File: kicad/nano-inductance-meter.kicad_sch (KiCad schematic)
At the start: 27 parts, among them J6 NOKIA5110_LCD, SW1 Calibrate, U1 MCP6004

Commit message: update
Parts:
- C2: value 100n -> 100nF
- Cref1: renamed from Cref; value 470n -> 470nF
- renumbered J6 to J1, JP2 to JP1, JP1 to JP2, Lx to Lx1, R19 to R10, R20 to R11, R21 to R12, R22 to R13, R7 to R2, R6 to R3, R2 to R4, R3 to R5, R4 to R6, R5 to R7, R17 to R8, R18 to R9
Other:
- note added: "Erősítő ~11x (~158Hz-től)"
- note added: "Schmitt-trigger"
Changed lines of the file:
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@@
 		(company "BT-Soft")
 	)
+	(text "Schmitt-trigger"
+		(exclude_from_sim no)
+		(at 161.29 48.006 0)
+		(effects
+			(font
+				(size 1.27 1.27)
+			)
+		)
+	)
 	(text "Vcc/2 (Vref)"
 		(exclude_from_sim no)
-		(at 118.364 71.374 0)
+		(at 118.872 96.012 0)
+		(effects
+			(font
+				(size 1.27 1.27)
+			)
+		)
+	)
+	(text "Erősítő ~11x\n(~158Hz-től)"
+		(exclude_from_sim no)
+		(at 126.746 53.086 0)
 		(effects
 			(font
@@
 		(on_board yes)
 		(dnp no)
-		(property "Reference" "J6"
+		(property "Reference" "J1"
 			(at 182.88 96.52 0)
 			(effects
@@
 			(project "nano-inductance-meter"
 				(path "/d4d5a955-4390-4c0c-a531-39dbbfc584c9"
-					(reference "J6")
+					(reference "J1")
 					(unit 1)
 				)
@@
 		(on_board yes)
 		(dnp no)
-		(property "Reference" "#PWR0131"
+		(property "Reference" "#PWR011"
 			(at 175.26 104.14 0)
 			(effects
@@
 			(project "nano-inductance-meter"
 				(path "/d4d5a955-4390-4c0c-a531-39dbbfc584c9"
-					(reference "#PWR0131")
+					(reference "#PWR011")
 					(unit 1)
 				)
@@
 		(on_board yes)
 		(dnp no)
-		(property "Reference" "R22"
+		(property "Reference" "R13"
 			(at 166.37 91.44 90)
 			(effects
@@
 			(project "nano-inductance-meter"
 				(path "/d4d5a955-4390-4c0c-a531-39dbbfc584c9"
-					(reference "R22")
+					(reference "R13")
 					(unit 1)
 				)
@@
 		(on_board yes)
 		(dnp no)
-		(property "Reference" "JP2"
+		(property "Reference" "JP1"
 			(at 148.1328 86.4616 90)
 			(effects
@@
 			(project "nano-inductance-meter"
 				(path "/d4d5a955-4390-4c0c-a531-39dbbfc584c9"
-					(reference "JP2")
+					(reference "JP1")
 					(unit 1)
 				)
@@
 		(on_board yes)
 		(dnp no)
-		(property "Reference" "#PWR0132"
+		(property "Reference" "#PWR09"
 			(at 147.32 95.25 0)
 			(effects
@@
 			(project "nano-inductance-meter"
 				(path "/d4d5a955-4390-4c0c-a531-39dbbfc584c9"
-					(reference "#PWR0132")
+					(reference "#PWR09")
 					(unit 1)
 				)
@@
 		(on_board yes)
 		(dnp no)
-		(property "Reference" "#PWR0133"
+		(property "Reference" "#PWR08"
 			(at 146.05 81.28 0)
 			(effects
@@
 			(project "nano-inductance-meter"
 				(path "/d4d5a955-4390-4c0c-a531-39dbbfc584c9"
-					(reference "#PWR0133")
+					(reference "#PWR08")
 					(unit 1)
 				)
@@
 		(on_board yes)
 		(dnp no)
-		(property "Reference" "R17"
+		(property "Reference" "R8"
 			(at 186.69 74.93 90)
 			(effects
@@
 			(project "nano-inductance-meter"
 				(path "/d4d5a955-4390-4c0c-a531-39dbbfc584c9"
-					(reference "R17")
+					(reference "R8")
 					(unit 1)
 				)
@@
 		(on_board yes)
 		(dnp no)
-		(property "Reference" "R18"
+		(property "Reference" "R9"
 			(at 186.69 77.47 90)
 			(effects
@@
 			(project "nano-inductance-meter"
 				(path "/d4d5a955-4390-4c0c-a531-39dbbfc584c9"
-					(reference "R18")
+					(reference "R9")
 					(unit 1)
 				)
@@
 		(on_board yes)
 		(dnp no)
-		(property "Reference" "R19"
+		(property "Reference" "R10"
 			(at 186.69 80.01 90)
 			(effects
@@
 			(project "nano-inductance-meter"
 				(path "/d4d5a955-4390-4c0c-a531-39dbbfc584c9"
-					(reference "R19")
+					(reference "R10")
 					(unit 1)
 				)
@@
 		(on_board yes)
 		(dnp no)
-		(property "Reference" "R20"
+		(property "Reference" "R11"
 			(at 186.69 82.55 90)
 			(effects
@@
 			(project "nano-inductance-meter"
 				(path "/d4d5a955-4390-4c0c-a531-39dbbfc584c9"
-					(reference "R20")
+					(reference "R11")
 					(unit 1)
 				)
@@
 		(on_board yes)
 		(dnp no)
-		(property "Reference" "R21"
+		(property "Reference" "R12"
 			(at 186.69 85.09 90)
 			(effects
@@
 			(project "nano-inductance-meter"
 				(path "/d4d5a955-4390-4c0c-a531-39dbbfc584c9"
-					(reference "R21")
+					(reference "R12")
 					(unit 1)
 				)
@@
 		(on_board yes)
 		(dnp no)
-		(property "Reference" "JP1"
+		(property "Reference" "JP2"
 			(at 171.45 69.723 0)
 			(effects
@@
 			(project "nano-inductance-meter"
 				(path "/d4d5a955-4390-4c0c-a531-39dbbfc584c9"
-					(reference "JP1")
+					(reference "JP2")
 					(unit 1)
 				)
@@
 		(dnp no)
 		(fields_autoplaced yes)
-		(property "Reference" "R6"
+		(property "Reference" "R3"
 			(at 90.17 96.5199 0)
 			(effects
@@
 			(project "nano-inductance-meter"
 				(path "/d4d5a955-4390-4c0c-a531-39dbbfc584c9"
-					(reference "R6")
+					(reference "R3")
 					(unit 1)
 				)
@@
 		(dnp no)
 		(fields_autoplaced yes)
-		(property "Reference" "Cref"
+		(property "Reference" "Cref1"
 			(at 97.79 49.5299 0)
 			(effects
@@
 			)
 		)
-		(property "Value" "470n"
+		(property "Value" "470nF"
 			(at 97.79 52.0699 0)
 			(effects
@@
 			(project "nano-inductance-meter"
 				(path "/d4d5a955-4390-4c0c-a531-39dbbfc584c9"
-					(reference "Cref")
+					(reference "Cref1")
 					(unit 1)
 				)
@@
 		(on_board yes)
 		(dnp no)
-		(property "Reference" "#PWR08"
+		(property "Reference" "#PWR03"
 			(at 53.34 45.72 0)
 			(effects
@@
 			(project "nano-inductance-meter"
 				(path "/d4d5a955-4390-4c0c-a531-39dbbfc584c9"
-					(reference "#PWR08")
+					(reference "#PWR03")
 					(unit 1)
 				)
@@
 		(on_board yes)
 		(dnp no)
-		(property "Reference" "#PWR09"
+		(property "Reference" "#PWR010"
 			(at 163.83 90.17 0)
 			(effects
@@
 			(project "nano-inductance-meter"
 				(path "/d4d5a955-4390-4c0c-a531-39dbbfc584c9"
-					(reference "#PWR09")
+					(reference "#PWR010")
 					(unit 1)
 				)
@@
 		(on_board yes)
 		(dnp no)
-		(property "Reference" "R5"
+		(property "Reference" "R7"
 			(at 149.352 23.114 90)
 			(effects
@@
 			(project "nano-inductance-meter"
 				(path "/d4d5a955-4390-4c0c-a531-39dbbfc584c9"
-					(reference "R5")
+					(reference "R7")
 					(unit 1)
 				)
@@
 		(dnp no)
 		(fields_autoplaced yes)
-		(property "Reference" "R7"
+		(property "Reference" "R2"
 			(at 90.17 82.5499 0)
 			(effects
@@
 			(project "nano-inductance-meter"
 				(path "/d4d5a955-4390-4c0c-a531-39dbbfc584c9"
-					(reference "R7")
+					(reference "R2")
 					(unit 1)
 				)
@@
 		(dnp no)
 		(fields_autoplaced yes)
-		(property "Reference" "Lx"
+		(property "Reference" "Lx1"
 			(at 81.28 49.5299 0)
 			(effects
@@
 			(project ""
 				(path "/d4d5a955-4390-4c0c-a531-39dbbfc584c9"
-					(reference "Lx")
+					(reference "Lx1")
 					(unit 1)
 				)
@@
 			)
 		)
-		(property "Value" "100n"
+		(property "Value" "100nF"
 			(at 115.57 64.7699 0)
 			(effects
@@
 		(dnp no)
 		(fields_autoplaced yes)
-		(property "Reference" "R2"
+		(property "Reference" "R4"
 			(at 114.3 53.3399 0)
 			(effects
@@
 			(project "nano-inductance-meter"
 				(path "/d4d5a955-4390-4c0c-a531-39dbbfc584c9"
-					(reference "R2")
+					(reference "R4")
 					(unit 1)
 				)
@@
 		(on_board yes)
 		(dnp no)
-		(property "Reference" "#PWR02"
+		(property "Reference" "#PWR06"
 			(at 87.63 80.01 0)
 			(effects
@@
 			(project ""
 				(path "/d4d5a955-4390-4c0c-a531-39dbbfc584c9"
-					(reference "#PWR02")
+					(reference "#PWR06")
 					(unit 1)
 				)
@@
 		(dnp no)
 		(fields_autoplaced yes)
-		(property "Reference" "R4"
+		(property "Reference" "R6"
 			(at 134.62 31.75 90)
 			(effects
@@
 			(project "nano-inductance-meter"
 				(path "/d4d5a955-4390-4c0c-a531-39dbbfc584c9"
-					(reference "R4")
+					(reference "R6")
 					(unit 1)
 				)
@@
 		(dnp no)
 		(fields_autoplaced yes)
-		(property "Reference" "#PWR04"
+		(property "Reference" "#PWR05"
 			(at 77.47 113.03 0)
 			(effects
@@
 			(project "nano-inductance-meter"
 				(path "/d4d5a955-4390-4c0c-a531-39dbbfc584c9"
-					(reference "#PWR04")
+					(reference "#PWR05")
 					(unit 1)
 				)
@@
 		(dnp no)
 		(fields_autoplaced yes)
-		(property "Reference" "R3"
+		(property "Reference" "R5"
 			(at 121.92 41.91 90)
 			(effects
@@
 			(project "nano-inductance-meter"
 				(path "/d4d5a955-4390-4c0c-a531-39dbbfc584c9"
-					(reference "R3")
+					(reference "R5")
 					(unit 1)
 				)
@@
 		(dnp no)
 		(fields_autoplaced yes)
-		(property "Reference" "#PWR06"
+		(property "Reference" "#PWR02"
 			(at 52.07 107.95 0)
 			(effects
@@
 			(project "nano-inductance-meter"
 				(path "/d4d5a955-4390-4c0c-a531-39dbbfc584c9"
-					(reference "#PWR06")
+					(reference "#PWR02")
 					(unit 1)
 				)
@@
 		(on_board yes)
 		(dnp no)
-		(property "Reference" "#PWR05"
+		(property "Reference" "#PWR04"
 			(at 55.88 45.72 0)
 			(effects
@@
 			(project "nano-inductance-meter"
 				(path "/d4d5a955-4390-4c0c-a531-39dbbfc584c9"
-					(reference "#PWR05")
+					(reference "#PWR04")
 					(unit 1)
 				)
@@
 		(dnp no)
 		(fields_autoplaced yes)
-		(property "Reference" "#PWR07"
+		(property "Reference" "#PWR01"
 			(at 22.86 67.31 0)
 			(effects
@@
 			(project "nano-inductance-meter"
 				(path "/d4d5a955-4390-4c0c-a531-39dbbfc584c9"
-					(reference "#PWR07")
+					(reference "#PWR01")
 					(unit 1)
 				)
@@
 		(dnp no)
 		(fields_autoplaced yes)
-		(property "Reference" "#PWR03"
+		(property "Reference" "#PWR07"
 			(at 87.63 113.03 0)
 			(effects
@@
 			(project ""
 				(path "/d4d5a955-4390-4c0c-a531-39dbbfc584c9"
-					(reference "#PWR03")
+					(reference "#PWR07")
 					(unit 1)
 				)

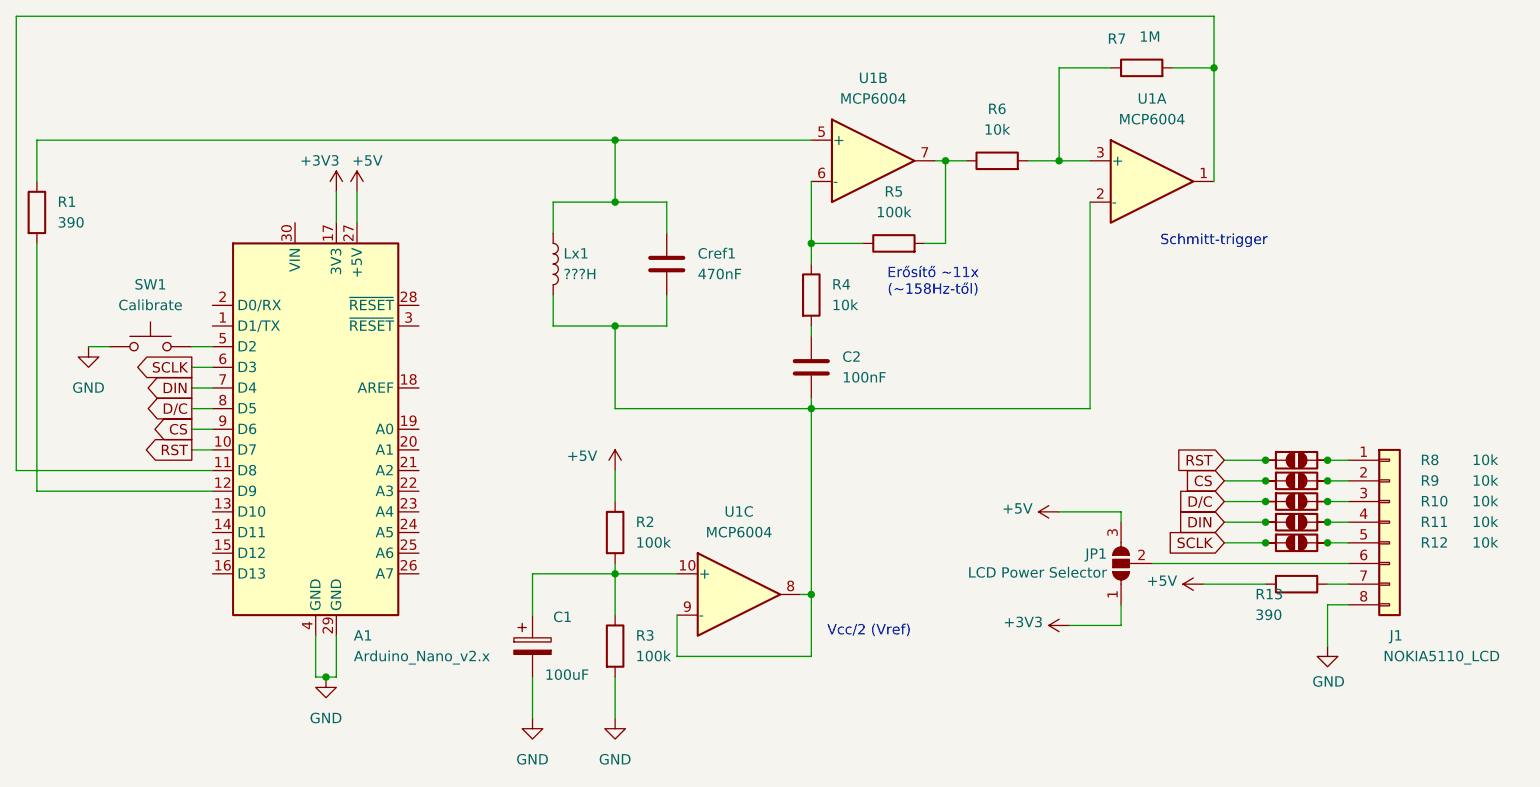
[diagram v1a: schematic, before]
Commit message: Update main.cpp and schematics.png
- Refactored code for better readability in main.cpp by adjusting spacing and formatting.
- Increased LCD contrast setting from 30 to 65 for improved display visibility.
- Updated schematics.png to reflect recent changes.
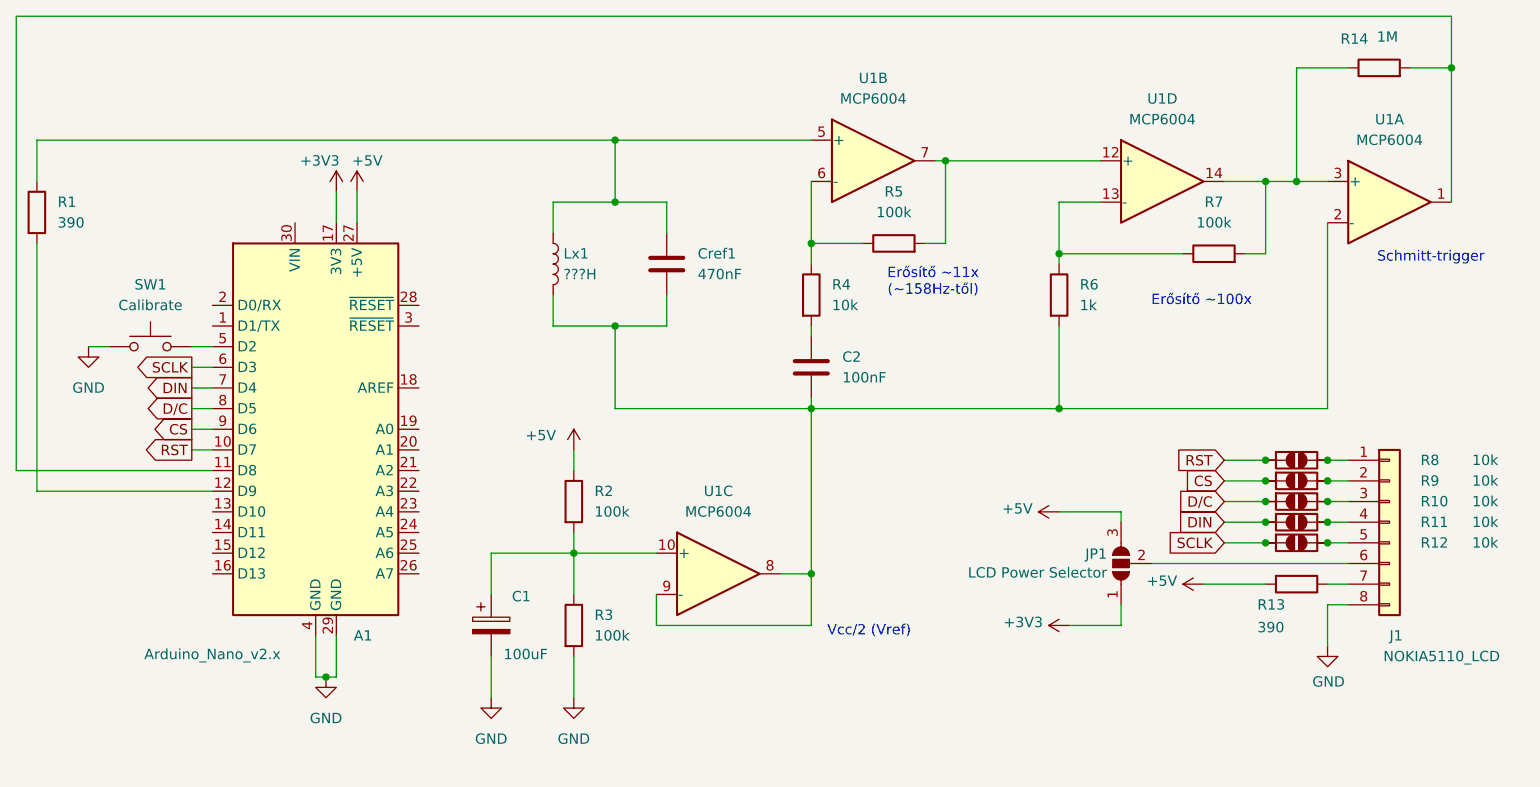
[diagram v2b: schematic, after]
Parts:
- added R7: 100k, Resistor_THT:R_Axial_DIN0207_L6.3mm_D2.5mm_P10.16mm_Horizontal, symbol Device:R
- added unit 4 of U1
- R6: value 10k -> 1k
- renumbered R7 to R14
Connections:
- net at C2.2, Cref1.2, Lx1.2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: now also R6.2
- net at R14.1, U1.3 (+): now also R7.2, U1.14; no longer R6.2
- net at R5.2, U1.7: now also U1.12 (+); no longer R6.1
- new net: R6.1, R7.1, U1.13 (-)
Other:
- note added: "Erősítő ~100x"
- moved on the sheet: C1, R14, R2, R3, U1A, U1C
